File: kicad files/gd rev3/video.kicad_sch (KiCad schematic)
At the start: 55 parts, among them J17 VGA_Micro, J18 vga_SWD, J22 L77HDE15SD1CH4F, SW6 Boot Sel, SW7 VGA RESET, U19 W25Q128JVS, U22 74HCT245, U23 RP2040, U24 74LVC2G04, U25 74LVC2G04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

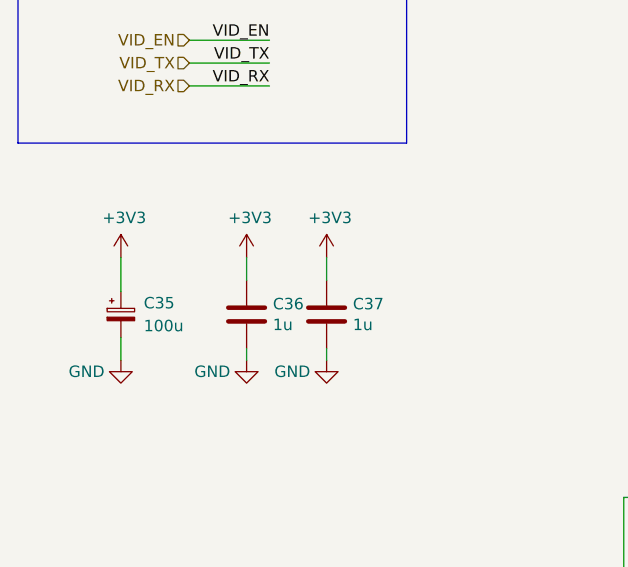
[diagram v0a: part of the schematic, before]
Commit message: colorized multi-sheet, other minor changes
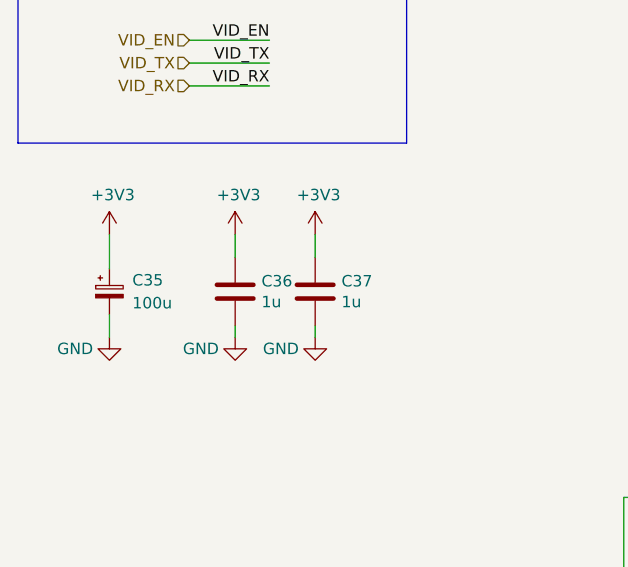
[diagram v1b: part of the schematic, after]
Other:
- moved on the sheet: C35, C36, C37

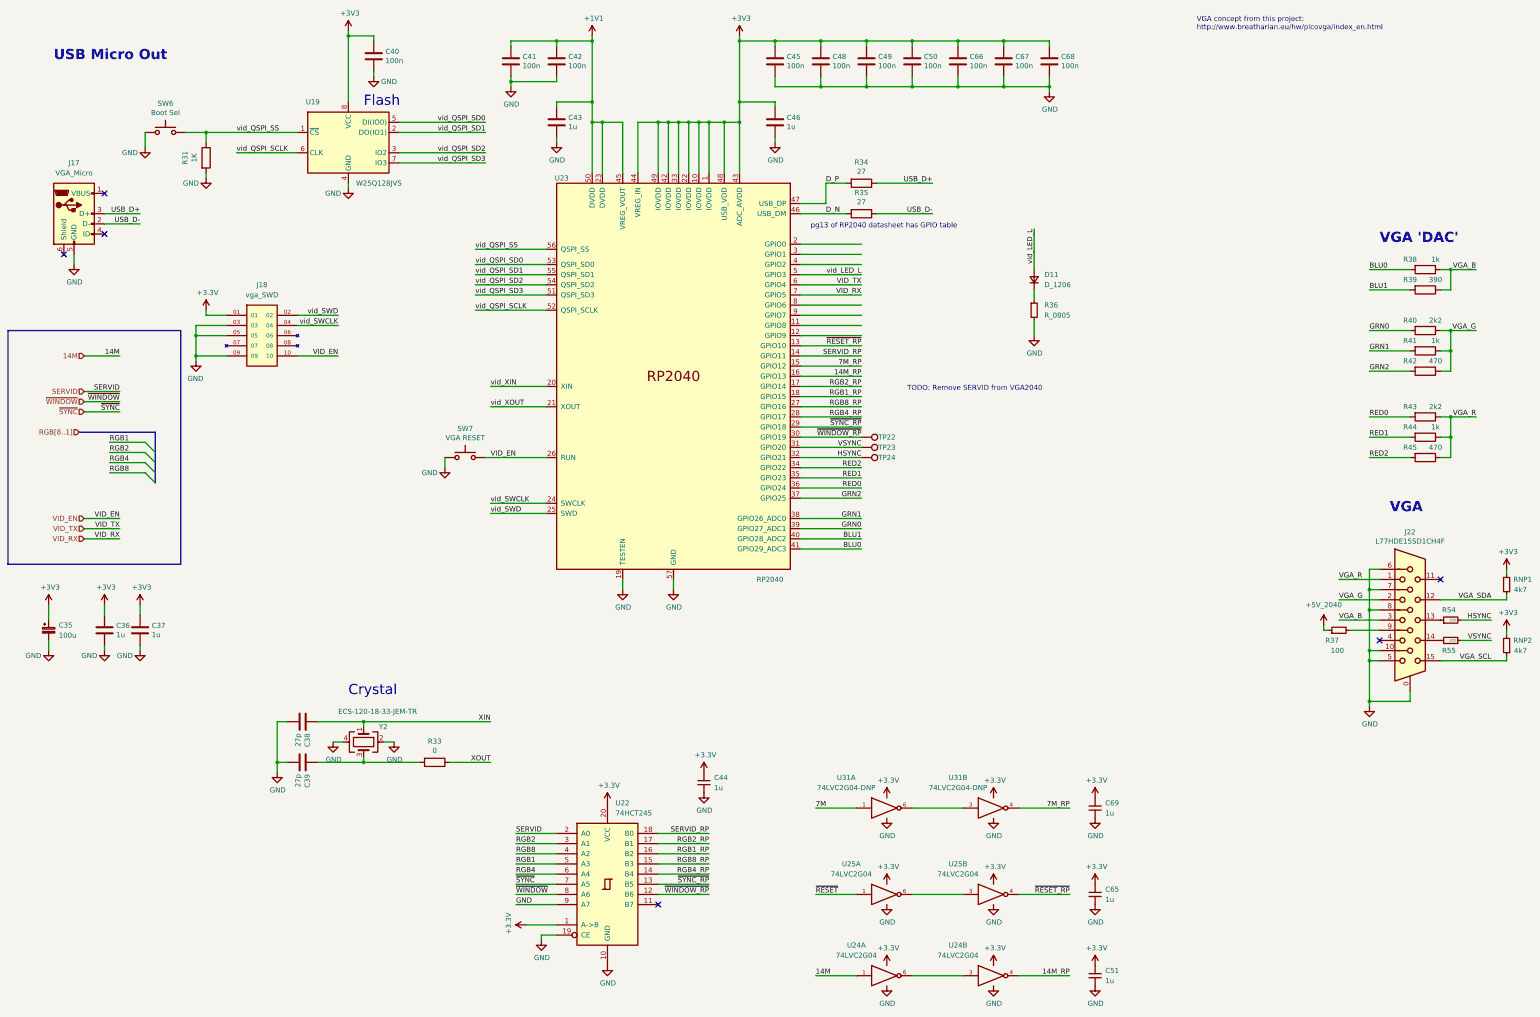
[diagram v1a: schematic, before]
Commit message: main grouping done now optimizing groups and locations
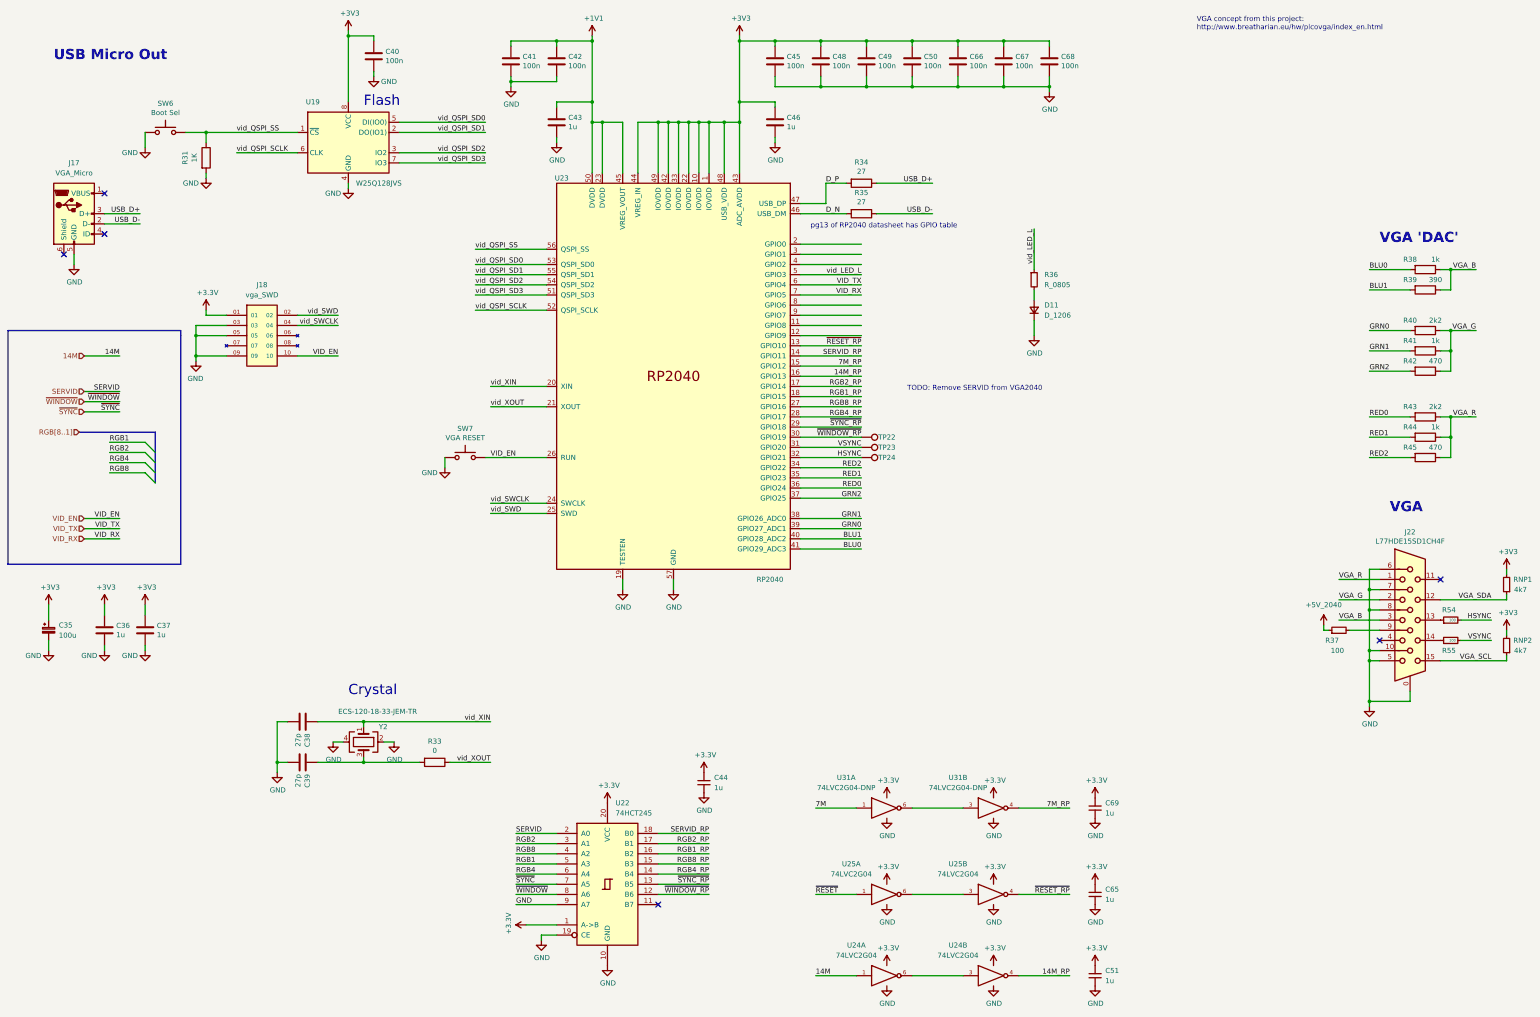
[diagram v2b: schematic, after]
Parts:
- TP22, TP23, TP24: footprint My Libraries:Harwin-S1751-46-Test-Point -> TestPoint:TestPoint_Pad_D1.0mm
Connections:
- net XIN is gone; now on net vid_XIN: C38.1, Y2.1
- net XOUT is gone; now on net vid_XOUT: R33.1
- net GND: now also D11.1 (K); no longer R36.2
- net vid_LED_L: now also R36.1; no longer D11.2 (A)
- new net: D11.2 (A), R36.2
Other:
- moved on the sheet: C37, D11, R36
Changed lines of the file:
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@@
     (stroke (width 0) (type default) (color 0 0 0 0))
   )
-  (wire (pts (xy 52.07 170.18) (xy 52.07 172.72))
+  (wire (pts (xy 53.34 170.18) (xy 53.34 172.72))
     (stroke (width 0) (type default) (color 0 0 0 0))
   )
@@
     (stroke (width 0) (type default) (color 0 0 0 0))
   )
-  (wire (pts (xy 52.07 180.34) (xy 52.07 181.61))
+  (wire (pts (xy 53.34 180.34) (xy 53.34 181.61))
     (stroke (width 0) (type default) (color 0 0 0 0))
   )
@@
     (effects (font (size 1.27 1.27)) (justify right bottom))
   )
-  (label "XOUT" (at 139.7 209.55 180)
+  (label "vid_XOUT" (at 139.7 209.55 180)
     (effects (font (size 1.27 1.27)) (justify right bottom))
   )
@@
     (effects (font (size 1.27 1.27)) (justify left bottom))
   )
-  (label "XIN" (at 139.7 199.39 180)
+  (label "vid_XIN" (at 139.7 199.39 180)
     (effects (font (size 1.27 1.27)) (justify right bottom))
   )
@@
     (pin "1")
   )
-  (symbol (lib_id "My Library:D_1206") (at 275.59 88.9 90) (unit 1)
+  (symbol (lib_id "My Library:D_1206") (at 275.59 96.52 90) (unit 1)
     (in_bom yes) (on_board yes) (fields_autoplaced)
-    (property "Reference" "D11" (id 0) (at 278.13 87.6299 90)
+    (property "Reference" "D11" (id 0) (at 278.13 95.2499 90)
       (effects (font (size 1.27 1.27)) (justify right))
     )
-    (property "Value" "D_1206" (id 1) (at 278.13 90.1699 90)
+    (property "Value" "D_1206" (id 1) (at 278.13 97.7899 90)
       (effects (font (size 1.27 1.27)) (justify right))
     )
-    (property "Footprint" "LED_SMD:LED_1206_3216Metric" (id 2) (at 275.59 88.9 90)
-      (effects (font (size 1.27 1.27)) hide)
-    )
-    (property "Datasheet" "~" (id 3) (at 275.59 88.9 90)
+    (property "Footprint" "LED_SMD:LED_1206_3216Metric" (id 2) (at 275.59 96.52 90)
+      (effects (font (size 1.27 1.27)) hide)
+    )
+    (property "Datasheet" "~" (id 3) (at 275.59 96.52 90)
       (effects (font (size 1.27 1.27)) hide)
     )
@@
       (effects (font (size 1.27 1.27)) hide)
     )
-    (property "Footprint" "My Libraries:Harwin-S1751-46-Test-Point" (id 2) (at 232.41 135.89 0)
+    (property "Footprint" "TestPoint:TestPoint_Pad_D1.0mm" (id 2) (at 232.41 135.89 0)
       (effects (font (size 1.27 1.27)) hide)
     )
@@
       (effects (font (size 1.27 1.27)) hide)
     )
-    (property "Footprint" "My Libraries:Harwin-S1751-46-Test-Point" (id 2) (at 232.41 138.43 0)
+    (property "Footprint" "TestPoint:TestPoint_Pad_D1.0mm" (id 2) (at 232.41 138.43 0)
       (effects (font (size 1.27 1.27)) hide)
     )
@@
     (pin "4")
   )
-  (symbol (lib_id "power:GND") (at 52.07 181.61 0) (unit 1)
-    (in_bom yes) (on_board yes)
-    (property "Reference" "#PWR0334" (id 0) (at 52.07 187.96 0)
-      (effects (font (size 1.27 1.27)) hide)
-    )
-    (property "Value" "GND" (id 1) (at 48.26 182.88 0))
-    (property "Footprint" "" (id 2) (at 52.07 181.61 0)
-      (effects (font (size 1.27 1.27)) hide)
-    )
-    (property "Datasheet" "" (id 3) (at 52.07 181.61 0)
+  (symbol (lib_id "power:GND") (at 53.34 181.61 0) (unit 1)
+    (in_bom yes) (on_board yes)
+    (property "Reference" "#PWR0334" (id 0) (at 53.34 187.96 0)
+      (effects (font (size 1.27 1.27)) hide)
+    )
+    (property "Value" "GND" (id 1) (at 49.53 182.88 0))
+    (property "Footprint" "" (id 2) (at 53.34 181.61 0)
+      (effects (font (size 1.27 1.27)) hide)
+    )
+    (property "Datasheet" "" (id 3) (at 53.34 181.61 0)
       (effects (font (size 1.27 1.27)) hide)
     )
@@
     (pin "1")
   )
-  (symbol (lib_id "power:+3V3") (at 52.07 170.18 0) (unit 1)
-    (in_bom yes) (on_board yes)
-    (property "Reference" "#PWR0335" (id 0) (at 52.07 173.99 0)
-      (effects (font (size 1.27 1.27)) hide)
-    )
-    (property "Value" "+3V3" (id 1) (at 52.451 165.7858 0))
-    (property "Footprint" "" (id 2) (at 52.07 170.18 0)
-      (effects (font (size 1.27 1.27)) hide)
-    )
-    (property "Datasheet" "" (id 3) (at 52.07 170.18 0)
+  (symbol (lib_id "power:+3V3") (at 53.34 170.18 0) (unit 1)
+    (in_bom yes) (on_board yes)
+    (property "Reference" "#PWR0335" (id 0) (at 53.34 173.99 0)
+      (effects (font (size 1.27 1.27)) hide)
+    )
+    (property "Value" "+3V3" (id 1) (at 53.721 165.7858 0))
+    (property "Footprint" "" (id 2) (at 53.34 170.18 0)
+      (effects (font (size 1.27 1.27)) hide)
+    )
+    (property "Datasheet" "" (id 3) (at 53.34 170.18 0)
       (effects (font (size 1.27 1.27)) hide)
     )
@@
     (pin "2")
   )
-  (symbol (lib_id "My Library:R_0805") (at 275.59 96.52 0) (unit 1)
+  (symbol (lib_id "My Library:R_0805") (at 275.59 88.9 0) (unit 1)
     (in_bom yes) (on_board yes) (fields_autoplaced)
-    (property "Reference" "R36" (id 0) (at 278.13 95.2499 0)
-      (effects (font (size 1.27 1.27)) (justify left))
-    )
-    (property "Value" "R_0805" (id 1) (at 278.13 97.7899 0)
-      (effects (font (size 1.27 1.27)) (justify left))
-    )
-    (property "Footprint" "Resistor_SMD:R_0805_2012Metric" (id 2) (at 275.59 96.52 0)
-      (effects (font (size 1.27 1.27)) hide)
-    )
-    (property "Datasheet" "~" (id 3) (at 275.59 96.52 0)
+    (property "Reference" "R36" (id 0) (at 278.13 87.6299 0)
+      (effects (font (size 1.27 1.27)) (justify left))
+    )
+    (property "Value" "R_0805" (id 1) (at 278.13 90.1699 0)
+      (effects (font (size 1.27 1.27)) (justify left))
+    )
+    (property "Footprint" "Resistor_SMD:R_0805_2012Metric" (id 2) (at 275.59 88.9 0)
+      (effects (font (size 1.27 1.27)) hide)
+    )
+    (property "Datasheet" "~" (id 3) (at 275.59 88.9 0)
       (effects (font (size 1.27 1.27)) hide)
     )
@@
     (pin "2")
   )
-  (symbol (lib_id "Device:C") (at 52.07 176.53 0) (unit 1)
-    (in_bom yes) (on_board yes)
-    (property "Reference" "C37" (id 0) (at 54.991 175.3616 0)
-      (effects (font (size 1.27 1.27)) (justify left))
-    )
-    (property "Value" "1u" (id 1) (at 54.991 177.673 0)
-      (effects (font (size 1.27 1.27)) (justify left))
-    )
-    (property "Footprint" "Capacitor_SMD:C_0805_2012Metric" (id 2) (at 53.0352 180.34 0)
-      (effects (font (size 1.27 1.27)) hide)
-    )
-    (property "Datasheet" "~" (id 3) (at 52.07 176.53 0)
+  (symbol (lib_id "Device:C") (at 53.34 176.53 0) (unit 1)
+    (in_bom yes) (on_board yes)
+    (property "Reference" "C37" (id 0) (at 56.261 175.3616 0)
+      (effects (font (size 1.27 1.27)) (justify left))
+    )
+    (property "Value" "1u" (id 1) (at 56.261 177.673 0)
+      (effects (font (size 1.27 1.27)) (justify left))
+    )
+    (property "Footprint" "Capacitor_SMD:C_0805_2012Metric" (id 2) (at 54.3052 180.34 0)
+      (effects (font (size 1.27 1.27)) hide)
+    )
+    (property "Datasheet" "~" (id 3) (at 53.34 176.53 0)
       (effects (font (size 1.27 1.27)) hide)
     )
@@
       (effects (font (size 1.27 1.27)) hide)
     )
-    (property "Footprint" "My Libraries:Harwin-S1751-46-Test-Point" (id 2) (at 232.41 133.35 0)
-      (effects (font (size 1.27 1.27)) hide)
-    )
+    (property "Footprint" "TestPoint:TestPoint_Pad_D1.0mm" (id 2) (at 232.41 133.35 0)
+      (effects (font (size 1.27 1.27)) hide)
+    )

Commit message: stream cleanup
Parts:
- removed R31: 1K, Resistor_SMD:R_0603_1608Metric, symbol Device:R
- added R73: 1K, Resistor_SMD:R_0603_1608Metric, symbol Device:R
- SW6: value Boot Sel -> VGA Boot Sel
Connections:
- net vid_QSPI_SS: now also R73.2; no longer SW6.2
- new net: R73.1, SW6.2
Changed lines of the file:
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@@
   (junction (at 359.41 171.45) (diameter 0) (color 0 0 0 0)
-  )
-  (junction (at 68.58 52.07) (diameter 0) (color 0 0 0 0)
   )
   (junction (at 165.1 29.21) (diameter 0) (color 0 0 0 0)
@@
     (stroke (width 0) (type default) (color 0 0 0 0))
   )
+  (wire (pts (xy 63.5 52.07) (xy 66.04 52.07))
+    (stroke (width 0) (type default) (color 0 0 0 0))
+  )
   (wire (pts (xy 44.45 137.16) (xy 53.34 137.16))
     (stroke (width 0) (type default) (color 0 0 0 0))
@@
     (stroke (width 0) (type default) (color 0 0 0 0))
   )
+  (wire (pts (xy 73.66 52.07) (xy 91.44 52.07))
+    (stroke (width 0) (type default) (color 0 0 0 0))
+  )
   (wire (pts (xy 110.49 36.83) (xy 110.49 38.1))
     (stroke (width 0) (type default) (color 0 0 0 0))
@@
     (stroke (width 0) (type default) (color 0 0 0 0))
   )
-  (wire (pts (xy 68.58 52.07) (xy 91.44 52.07))
-    (stroke (width 0) (type default) (color 0 0 0 0))
-  )
   (wire (pts (xy 135.89 85.09) (xy 153.67 85.09))
     (stroke (width 0) (type default) (color 0 0 0 0))
@@
     (stroke (width 0) (type default) (color 0 0 0 0))
   )
-  (wire (pts (xy 68.58 62.23) (xy 68.58 63.5))
-    (stroke (width 0) (type default) (color 0 0 0 0))
-  )
   (wire (pts (xy 217.17 143.51) (xy 232.41 143.51))
     (stroke (width 0) (type default) (color 0 0 0 0))
@@
     (stroke (width 0) (type default) (color 0 0 0 0))
   )
-  (wire (pts (xy 68.58 52.07) (xy 68.58 54.61))
-    (stroke (width 0) (type default) (color 0 0 0 0))
-  )
   (wire (pts (xy 217.17 151.13) (xy 232.41 151.13))
     (stroke (width 0) (type default) (color 0 0 0 0))
@@
   )
   (wire (pts (xy 110.49 27.94) (xy 104.14 27.94))
-    (stroke (width 0) (type default) (color 0 0 0 0))
-  )
-  (wire (pts (xy 63.5 52.07) (xy 68.58 52.07))
     (stroke (width 0) (type default) (color 0 0 0 0))
   )
@@
     (pin "1")
   )
-  (symbol (lib_id "Device:R") (at 68.58 58.42 0) (unit 1)
-    (in_bom yes) (on_board yes)
-    (property "Reference" "R31" (id 0) (at 63.3222 58.42 90))
-    (property "Value" "1K" (id 1) (at 65.6336 58.42 90))
-    (property "Footprint" "Resistor_SMD:R_0603_1608Metric" (id 2) (at 66.802 58.42 90)
-      (effects (font (size 1.27 1.27)) hide)
-    )
-    (property "Datasheet" "~" (id 3) (at 68.58 58.42 0)
-      (effects (font (size 1.27 1.27)) hide)
-    )
-    (pin "1")
-    (pin "2")
-  )
   (symbol (lib_id "power:GND") (at 115.57 204.47 0) (unit 1)
     (in_bom yes) (on_board yes)
@@
     (in_bom yes) (on_board yes)
     (property "Reference" "SW6" (id 0) (at 58.42 44.831 0))
-    (property "Value" "Boot Sel" (id 1) (at 58.42 47.1424 0))
+    (property "Value" "VGA Boot Sel" (id 1) (at 58.42 47.1424 0))
     (property "Footprint" "Button_Switch_SMD:SW_SPST_PTS810" (id 2) (at 58.42 46.99 0)
       (effects (font (size 1.27 1.27)) hide)
@@
     (pin "2")
   )
+  (symbol (lib_id "Device:R") (at 69.85 52.07 90) (unit 1)
+    (in_bom yes) (on_board yes)
+    (property "Reference" "R73" (id 0) (at 69.85 57.3278 90))
+    (property "Value" "1K" (id 1) (at 69.85 55.0164 90))
+    (property "Footprint" "Resistor_SMD:R_0603_1608Metric" (id 2) (at 69.85 53.848 90)
+      (effects (font (size 1.27 1.27)) hide)
+    )
+    (property "Datasheet" "~" (id 3) (at 69.85 52.07 0)
+      (effects (font (size 1.27 1.27)) hide)
+    )
+    (pin "1")
+    (pin "2")
+  )
   (symbol (lib_id "Device:C") (at 156.21 34.29 0) (unit 1)
     (in_bom yes) (on_board yes)
@@
       (effects (font (size 1.27 1.27)) hide)
     )
-    (pin "1")
-  )
-  (symbol (lib_id "power:GND") (at 68.58 63.5 0) (unit 1)
-    (in_bom yes) (on_board yes)
-    (property "Reference" "#PWR0278" (id 0) (at 68.58 69.85 0)
-      (effects (font (size 1.27 1.27)) hide)
-    )
-    (property "Value" "GND" (id 1) (at 64.77 64.77 0))
-    (property "Footprint" "" (id 2) (at 68.58 63.5 0)
-      (effects (font (size 1.27 1.27)) hide)
-    )
-    (property "Datasheet" "" (id 3) (at 68.58 63.5 0)
-      (effects (font (size 1.27 1.27)) hide)
-    )
